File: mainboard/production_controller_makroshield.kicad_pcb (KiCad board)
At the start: 2 copper layers, 165.1 x 204 mm, 106 parts, among them J1 CON_TERM_BLK_1X2_TB008A-508-0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, J10 CON_CONNAXIO_MOTOR_DRIVER, J11 CON_CONNAXIO_MOTOR_DRIVER, J12 CON_CONNAXIO_MOTOR_DRIVER, J13 CON_CONNAXIO_MOTOR_DRIVER, J14 CON_CONNAXIO_MOTOR_DRIVER, J15 CON_CONNAXIO_MOTOR_DRIVER, J16 CON_CONNAXIO_MOTOR_DRIVER, J17 CON_CONNAXIO_MOTOR_DRIVER, J18 CON_CONNAXIO_MOTOR_DRIVER, J19 CON_CONNAXIO_MOTOR_DRIVER, J2 CON_TERM_BLK_1X2_TB008A-508-0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, J20 CON_CONNAXIO_MOTOR_DRIVER, J3 CON_HDR_MIKROBUS_ADDON_TH, J4 CON_TERM_BLK_1X2_TB008A-508-0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, J5 CON_HDR_MIKROBUS_SOCKET_TH, J6 CON_CONNAXIO_MOTOR_DRIVER, J7 CON_CONNAXIO_MOTOR_DRIVER, J8 CON_CONNAXIO_MOTOR_DRIVER, J9 CON_CONNAXIO_MOTOR_DRIVER, Q1 TRX_PMOS_AOD4189, Q2 TRX_2NPN_BC846S,115, U1 IO_EXP_PI4IOE5V6416ZDEX, U2 IO_EXP_PI4IOE5V6416ZDEX, U3 SUN_CUR_ACS711KEXLT-31AB-T, U4 ADC_NAU7802SGI

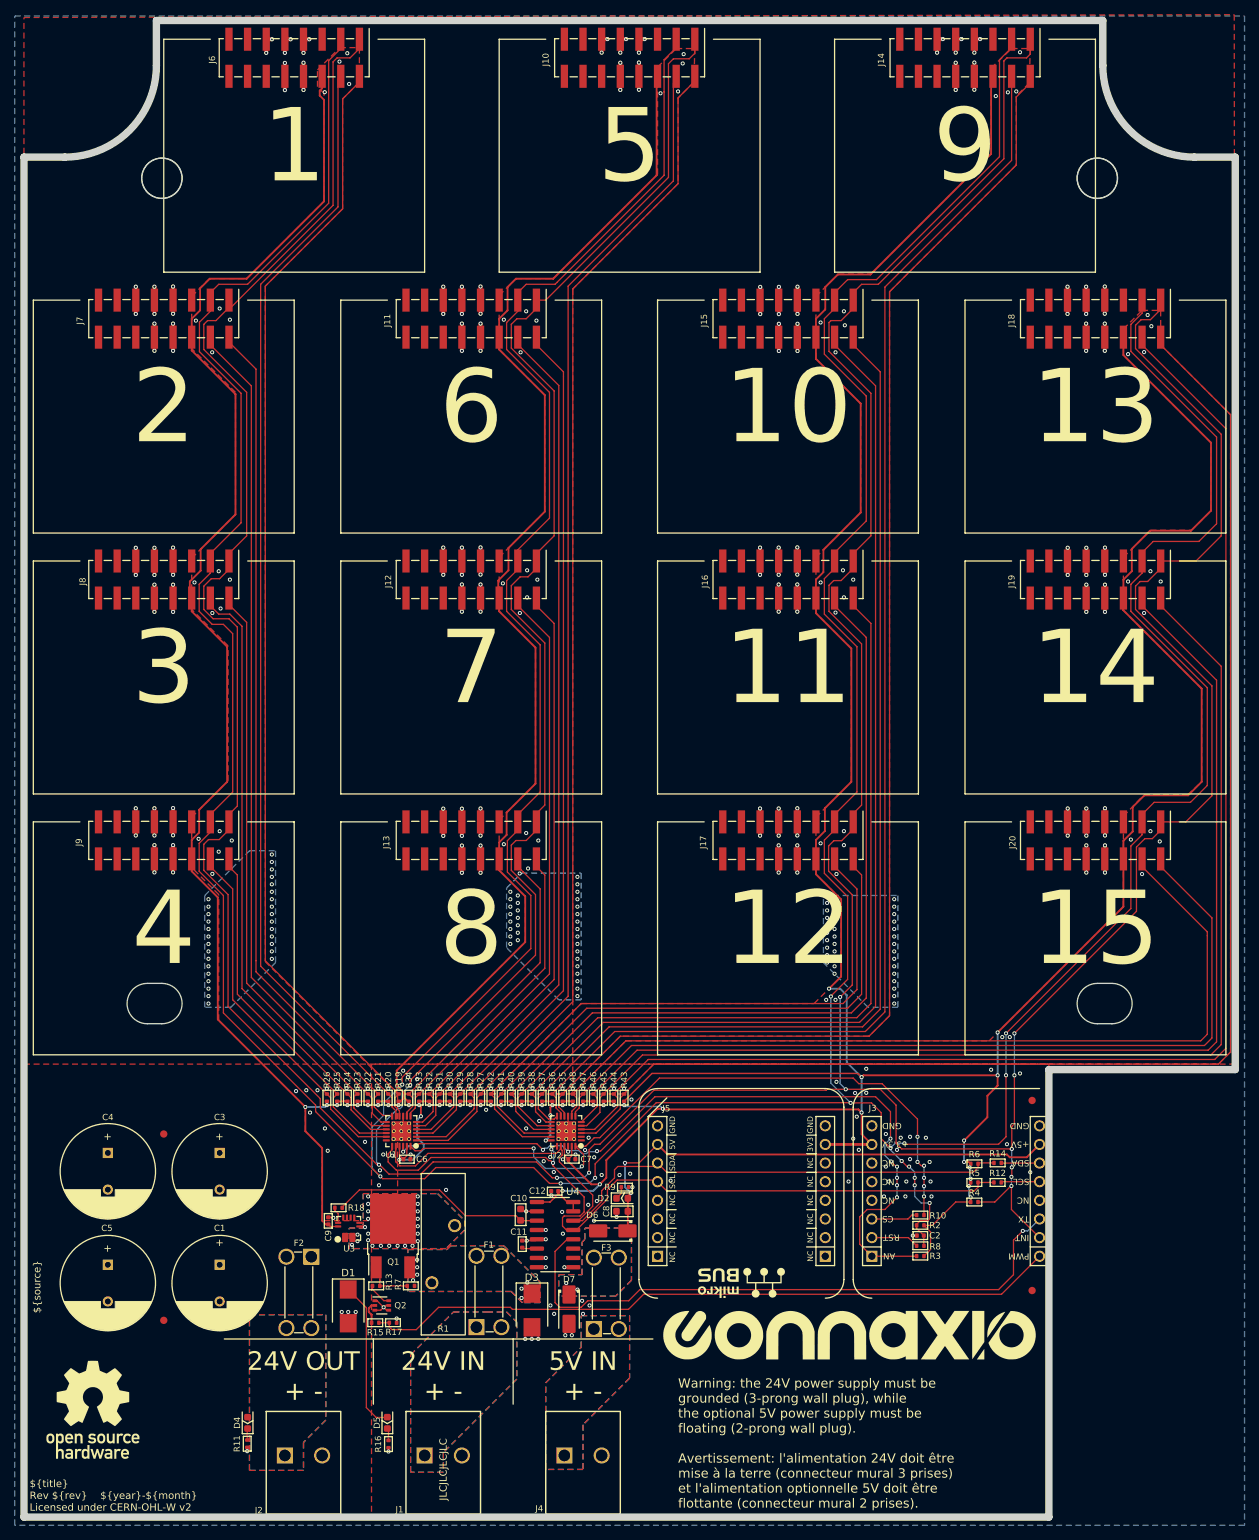
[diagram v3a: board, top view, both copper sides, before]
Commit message: Add onboard temperature sensor Add connector for Analog / 1-wire / PWM sensor
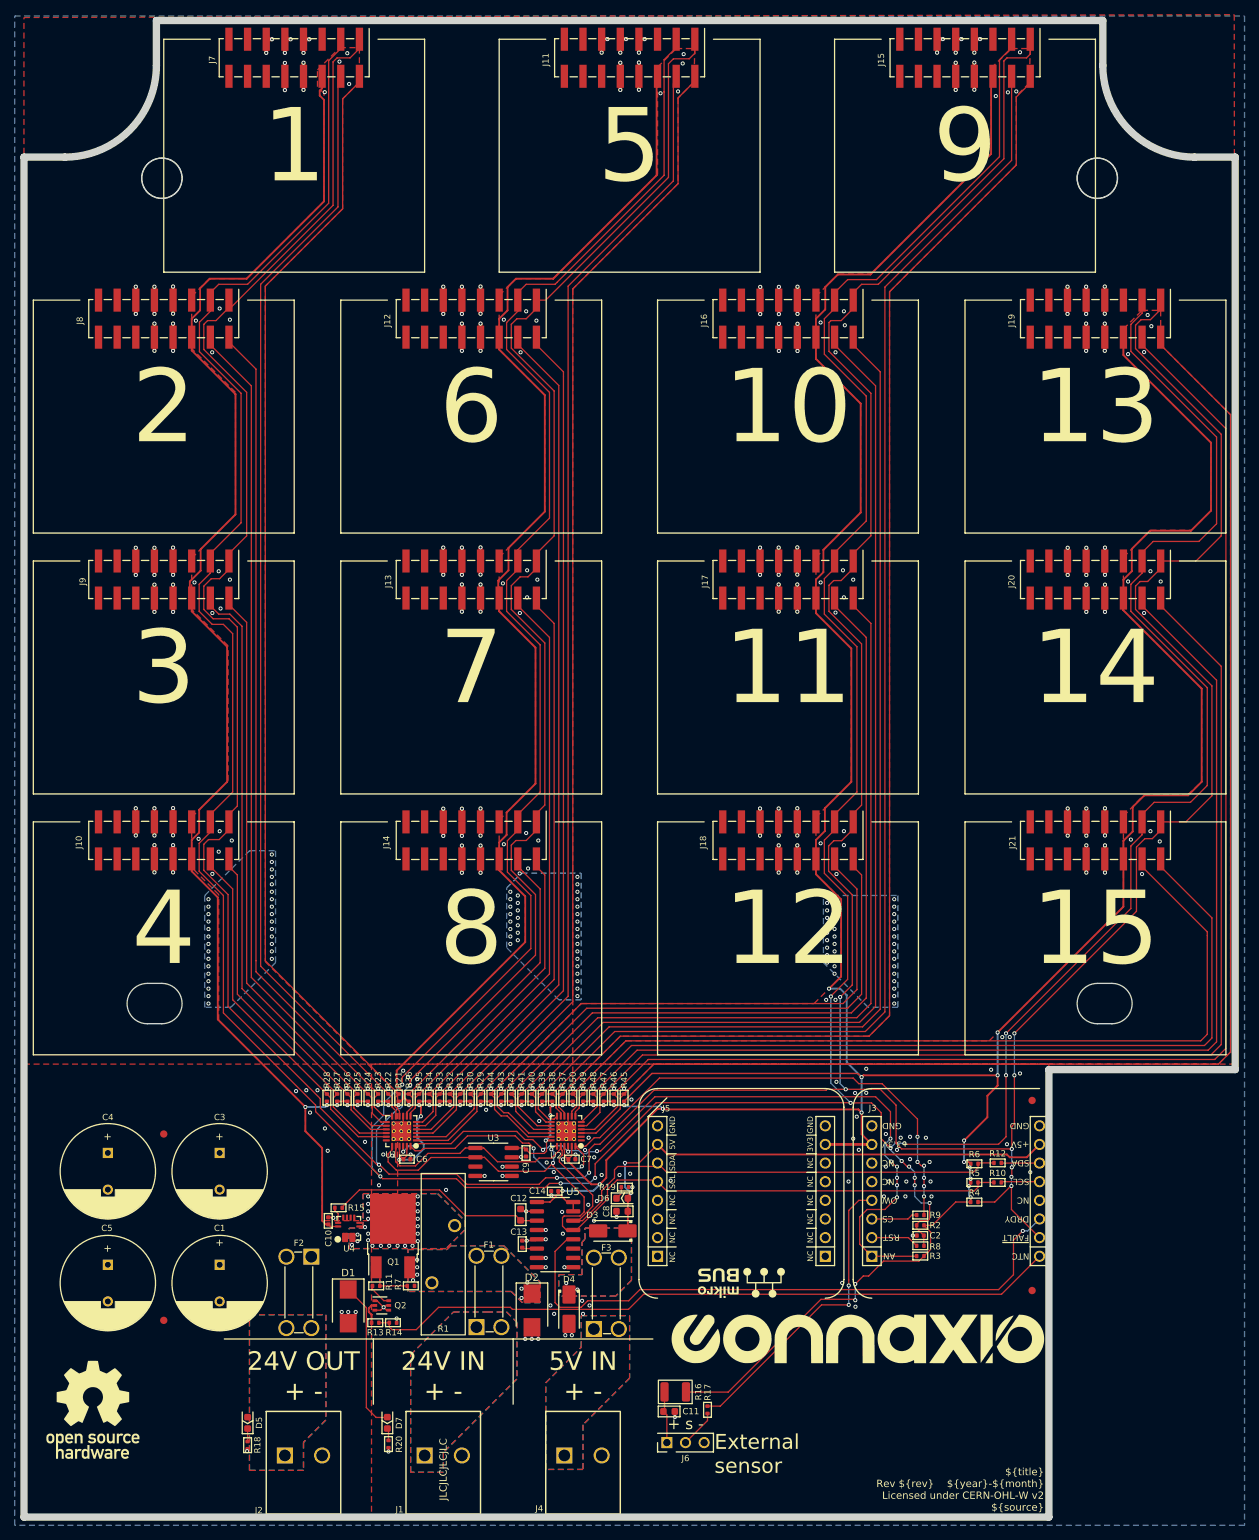
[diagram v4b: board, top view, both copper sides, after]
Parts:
- removed the D4 at (108.0, 224.3)
- removed the R11 at (108.0, 227.2)
- added C11: CAP_CER_22UF_10V_0603, connaxio-capacitors:CAP_CER_0603_1608M, F.Cu at (165.5, 222.8)
- added C9: CAP_CER_100NF_25V_0402, connaxio-capacitors:CAP_CER_0402_1005M, F.Cu at (146.0, 187.6)
- added D5: DIO_LED_GREEN_150060GS75000, connaxio-diodes:LED_0603_1608M, F.Cu at (108.0, 224.3)
- added J6: CON_HDR_100MILS_M_TH_1X3, connaxio-connectors:CON_HDR_100MILS_M_TH_1X3, F.Cu at (167.7, 227.0)
- added R16: PTC_SMD1210B010TF, connaxio-resistors:RES_1210_3225M, F.Cu at (166.3, 220.1)
- added R17: RES_226Ω_1%_0402, connaxio-resistors:RES_0402_1005M, F.Cu at (170.7, 222.6)
- added R18: RES_5.10KΩ_1%_0402, connaxio-resistors:RES_0402_1005M, F.Cu at (108.0, 227.4)
- added U3: SEN_TEMP_TMP1075DR, connaxio-sop:SOIC-8_3.9x4.9_P1.27, F.Cu at (141.6, 188.8)
- U4: renamed from U3; value SUN_CUR_ACS711KEXLT-31AB-T -> SEN_CUR_ACS711KEXLT-31AB-T
- moved G*** 1.25 mm to (191.2, 212.9)
- renumbered C9 to C10, C10 to C12, C11 to C13, C12 to C14, D3 to D2, D6 to D3, D7 to D4, D2 to D6, D5 to D7, J9 to J10, J10 to J11, J11 to J12, J12 to J13, J13 to J14, J14 to J15, J15 to J16, J16 to J17, J17 to J18, J18 to J19, J19 to J20, J20 to J21, J6 to J7, J7 to J8, J8 to J9, R12 to R10, R13 to R11, R14 to R12, R15 to R13, R17 to R14, R18 to R15, R9 to R19, R16 to R20, R19 to R21, R20 to R22, R21 to R23, R22 to R24, R23 to R25, R24 to R26, R25 to R27, R26 to R28, R27 to R29, R28 to R30, R29 to R31, R30 to R32, R31 to R33, R32 to R34, R33 to R35, R34 to R36, R35 to R37, R36 to R38, R37 to R39, R38 to R40, R39 to R41, R40 to R42, R41 to R43, R42 to R44, R43 to R45, R44 to R46, R45 to R47, R46 to R48, R47 to R49, R48 to R50, R10 to R9, U4 to U5
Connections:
- net Net-(D4-Pad2) renamed /24V_OUT
- J3 pad 4: unconnected-(J3-Pad4) -> /ONE_WIRE
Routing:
- net +3.3V: track 902.7 -> 950.9 mm, vias 49 -> 51
- net /ONE_WIRE: track 0.00 -> 41.6 mm, vias 0 -> 2
- net Net-(J6-Pad1): track 0.00 -> 7.17 mm
- net Net-(J6-Pad2): track 0.00 -> 5.21 mm
- net Net-(D5-Pad1): track 0.00 -> 1.77 mm
- net Net-(D4-Pad1): track 1.59 -> 0.00 mm
- net /I2C_SDA: track 102.3 -> 103.9 mm
- net /RST_IO: track 95.4 -> 96.9 mm
- net /INT_IO: track 104.7 -> 106.1 mm
- net /I2C_SCL: track 106.2 -> 107.2 mm
- net RST_MOT: track 803.4 -> 802.6 mm
- net FAULT: track 814.1 -> 813.4 mm
- net GND: track 297.4 -> 297.3 mm, vias 340 -> 345
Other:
- board text added: "${title} Rev ${rev} ${year}-${month} Licensed under CERN-OHL-W v2 ${source}"
- board text added: "+ s -"
- board text added: "External sensor"
- board text removed: "${source}"
- board text removed: "${title} Rev ${rev} ${year}-${month} Licensed under CERN-OHL-W v2"
